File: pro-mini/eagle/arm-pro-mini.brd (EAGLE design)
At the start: 38.1 x 20.3 mm, 61 parts, among them J1 MICRO USB, J2 SWD HEADER, Q1 12Mhz, T1 MMBT3906, U1 PRTR5V0U2X, U2 MIC5225-3.3v, U3 LPC11U35FHI33/501, U4 BAS40-05

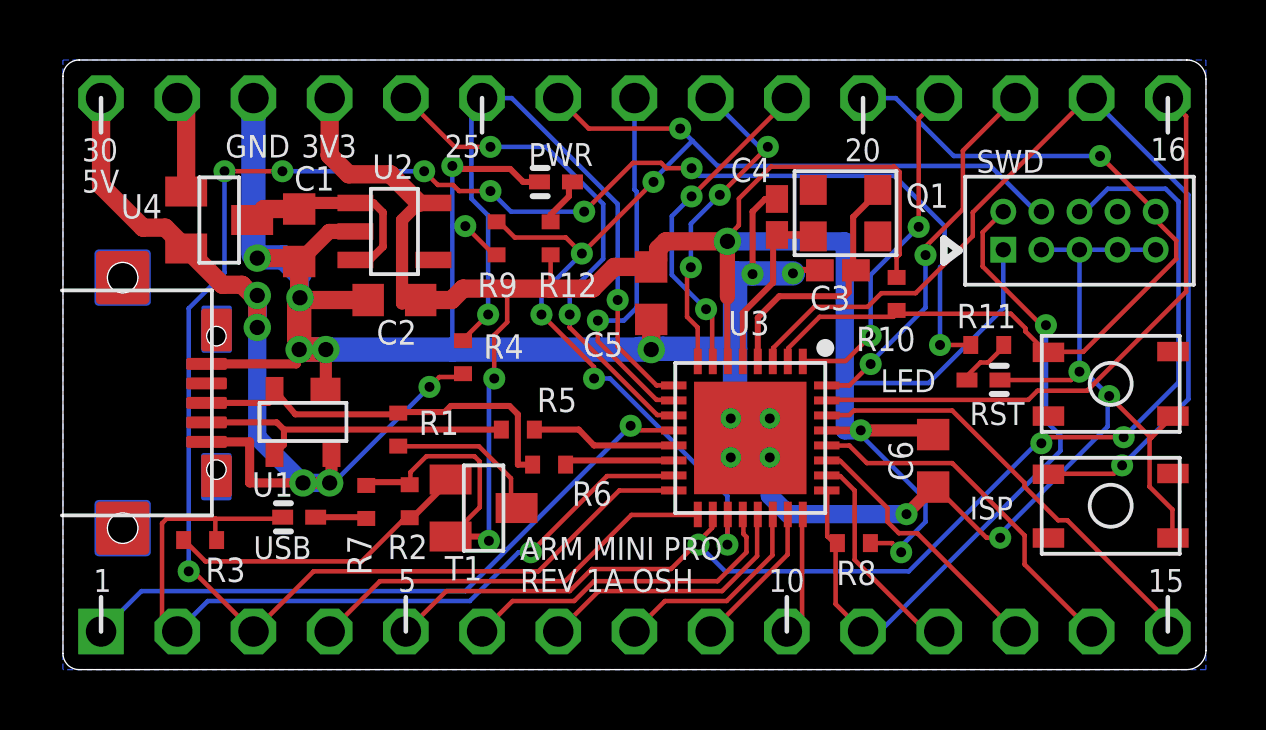
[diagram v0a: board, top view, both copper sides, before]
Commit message: Moved the SWD header slightly up to increase the clearance from the buttons.
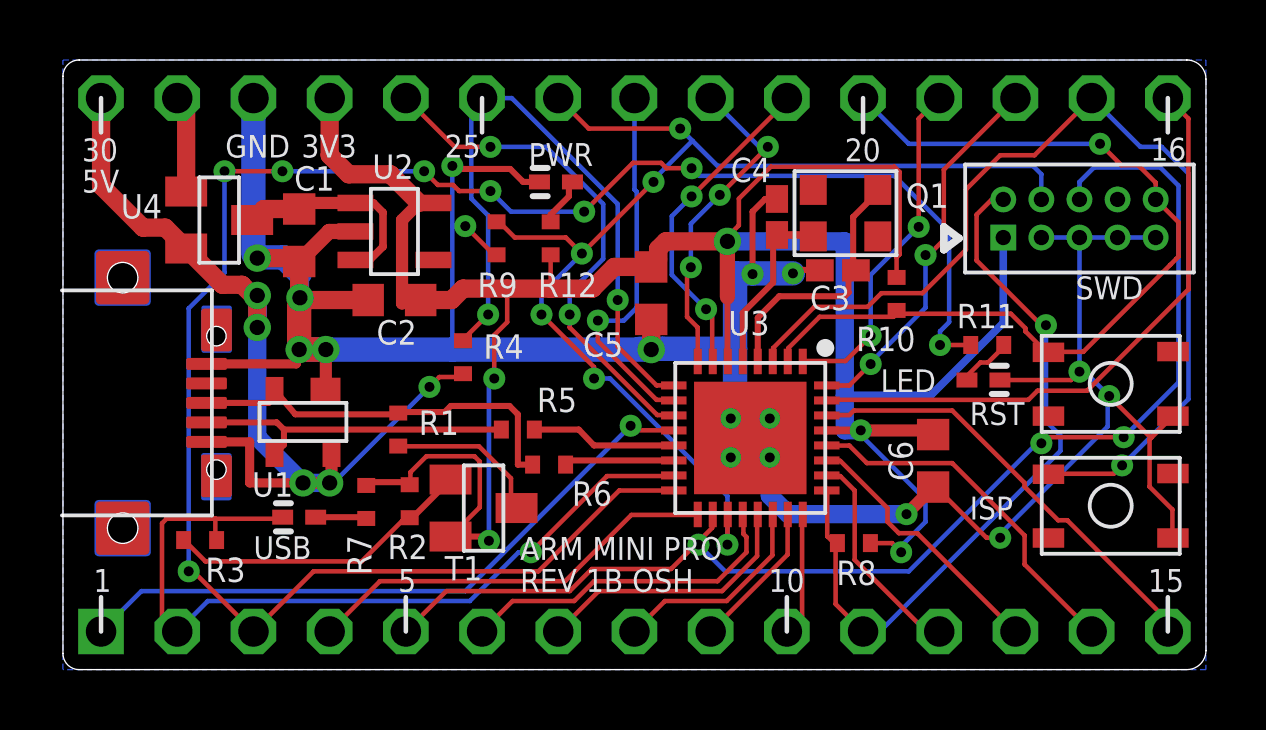
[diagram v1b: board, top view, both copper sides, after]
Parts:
- moved J2 0.41 mm to (33.9, 15.0)
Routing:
- net PIO0_1-ISP_EN: track 32.1 -> 33.3 mm
- net PIO0_9-SWDO: track 41.0 -> 42.0 mm
- net +3V3: track 84.3 -> 85.2 mm
- net PIO0_15-SWDIO: track 23.8 -> 24.6 mm
- net PIO0_0-RESET: track 29.1 -> 29.7 mm
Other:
- board text added: "REV 1B OSH"
- board text removed: "REV 1A OSH"
